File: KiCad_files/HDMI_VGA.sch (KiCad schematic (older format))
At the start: 64 parts, among them J5 TFP410, J6 DB15_Female_HighDensity_Mount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, J7 HDMI_A_1.4, U11 TPD12S521, U12 PCA9306

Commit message: Finished capacitor footprints
Total cost: ~$55
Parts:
- C214, C215, C216, C217: footprint (none) -> Capacitors_SMD:C_0201
- C228, C229: footprint (none) -> Capacitors_SMD:C_0402
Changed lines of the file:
@@
 F 0 "C214" H 7692 1396 50  0000 L CNN
 F 1 "0.1u" H 7692 1305 50  0000 L CNN
-F 2 "" H 7600 1350 50  0001 C CNN
+F 2 "Capacitors_SMD:C_0201" H 7600 1350 50  0001 C CNN
 F 3 "~" H 7600 1350 50  0001 C CNN
 	1    7600 1350
@@
 F 0 "C216" H 8392 1396 50  0000 L CNN
 F 1 "0.1u" H 8392 1305 50  0000 L CNN
-F 2 "" H 8300 1350 50  0001 C CNN
+F 2 "Capacitors_SMD:C_0201" H 8300 1350 50  0001 C CNN
 F 3 "~" H 8300 1350 50  0001 C CNN
 	1    8300 1350
@@
 F 0 "C215" H 8042 1396 50  0000 L CNN
 F 1 "0.1u" H 8042 1305 50  0000 L CNN
-F 2 "" H 7950 1350 50  0001 C CNN
+F 2 "Capacitors_SMD:C_0201" H 7950 1350 50  0001 C CNN
 F 3 "~" H 7950 1350 50  0001 C CNN
 	1    7950 1350
@@
 F 0 "C217" H 8742 1396 50  0000 L CNN
 F 1 "0.1u" H 8742 1305 50  0000 L CNN
-F 2 "" H 8650 1350 50  0001 C CNN
+F 2 "Capacitors_SMD:C_0201" H 8650 1350 50  0001 C CNN
 F 3 "~" H 8650 1350 50  0001 C CNN
 	1    8650 1350
@@
 F 0 "C228" H 6992 1396 50  0000 L CNN
 F 1 "1u" H 6992 1305 50  0000 L CNN
-F 2 "" H 6900 1350 50  0001 C CNN
+F 2 "Capacitors_SMD:C_0402" H 6900 1350 50  0001 C CNN
 F 3 "~" H 6900 1350 50  0001 C CNN
 	1    6900 1350
@@
 F 0 "C229" H 7342 1396 50  0000 L CNN
 F 1 "1u" H 7342 1305 50  0000 L CNN
-F 2 "" H 7250 1350 50  0001 C CNN
+F 2 "Capacitors_SMD:C_0402" H 7250 1350 50  0001 C CNN
 F 3 "~" H 7250 1350 50  0001 C CNN
 	1    7250 1350

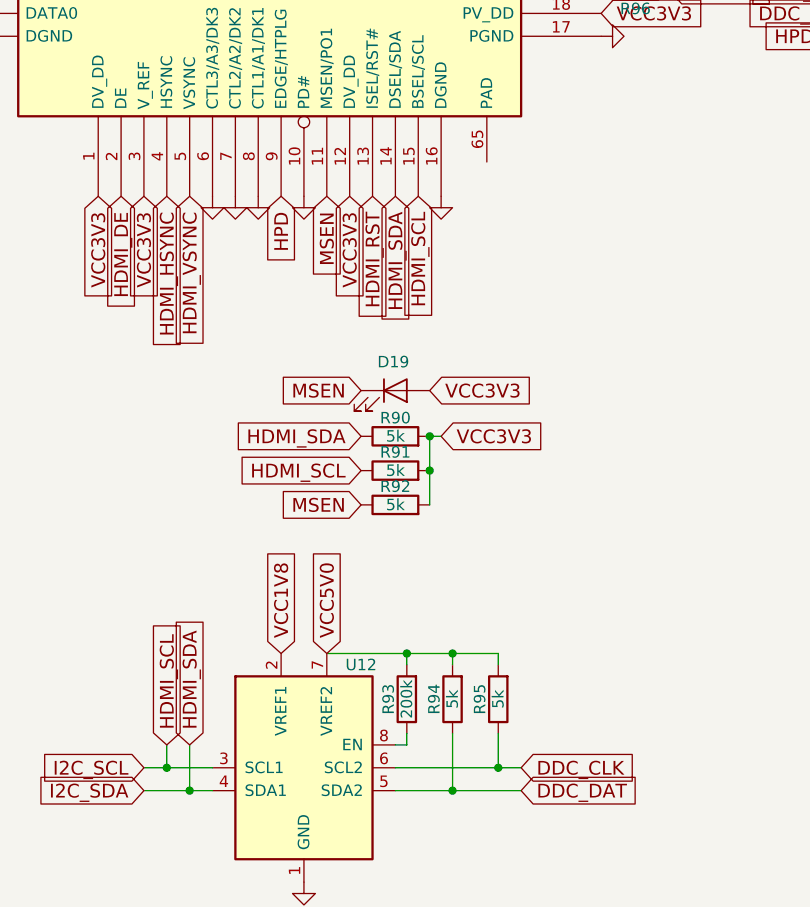
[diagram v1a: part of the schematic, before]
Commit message: Almost done with footprints. See issues below
Inductors left to do.
Others without footprints need custom.
PI3420 is out of stock...
LM2676 symbol should be re-drawn for TO-263-7
Total cost: ~$214
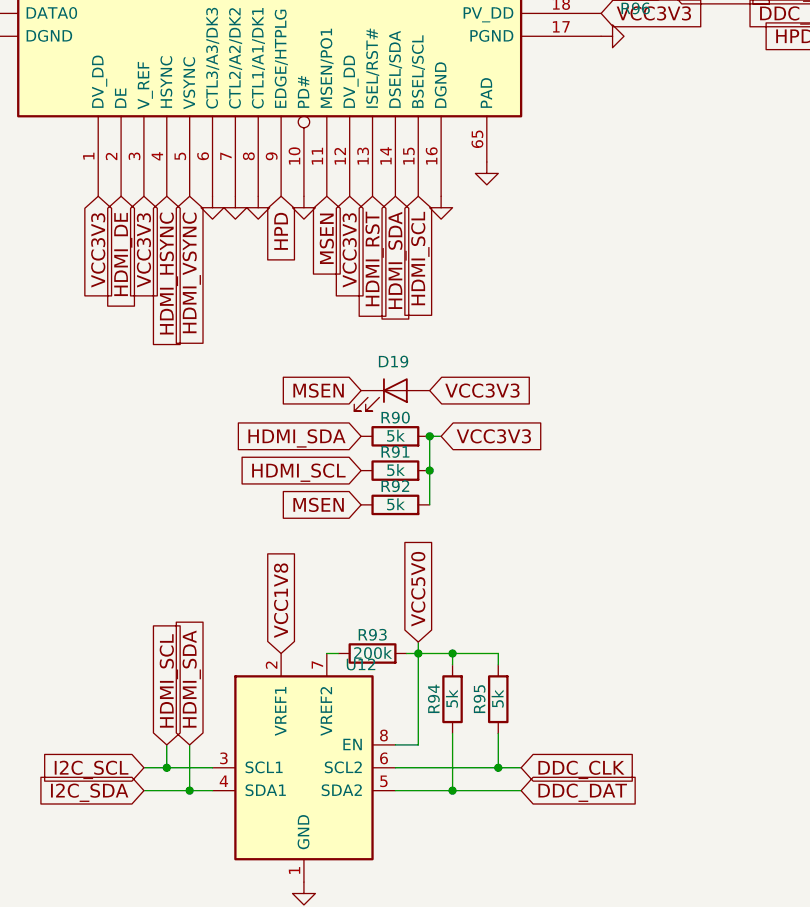
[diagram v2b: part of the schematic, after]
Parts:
- D19: footprint (none) -> LEDs:LED_0603
- J5: footprint (none) -> Housings_QFP:HTQFP-64-1EP_10x10mm_Pitch0.5mm_ThermalPad
- J6: footprint (none) -> Connectors_DSub:DSUB-15-HD_Female_Horizontal_Pitch2.29x1.98mm_EdgePinOffset3.03mm_Housed_MountingHolesOffset4.94mm
- R32, R33, R34, R35, R36, R37, R38, R39, R40, R41, R42, R43, R44, R45, R46, R47, R48, R49, R50, R51, R52, R53, R54, R55, R56, R57, R58, R59, R60, R61, R62, R63, R64, R65, R66, R67, R68, R69, R70, R71, R72, R73, R75, R90, R91, R92, R93, R94, R95, R96, R97: footprint (none) -> Resistors_SMD:R_0402
- R74: footprint (none) -> Resistors_SMD:R_0402_NoSilk
- U11: footprint (none) -> Housings_SSOP:TSSOP-38_4.4x9.7mm_Pitch0.5mm
- U12: footprint (none) -> Housings_SSOP:VSSOP-8_2.4x2.1mm_Pitch0.5mm
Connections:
- net GND: now also J5.65 (PAD)
- net VCC5V0: now also U12.8 (EN); no longer U12.7 (VREF2)
- net at R93.1: now also U12.7 (VREF2); no longer U12.8 (EN)
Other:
- moved on the sheet: R93

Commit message: Drew FPGA and HDMI footprints
Ready for layout...?
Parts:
- J7: footprint (none) -> custom:HDMI_A
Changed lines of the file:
@@
 F 0 "J7" H 10000 3850 50  0000 C CNN
 F 1 "HDMI_A_1.4" H 10650 3850 50  0000 C CNN
-F 2 "" H 10275 2800 50  0001 C CNN
+F 2 "custom:HDMI_A" H 10275 2800 50  0001 C CNN
 F 3 "" H 10275 2800 50  0001 C CNN
 	1    10250 2800
